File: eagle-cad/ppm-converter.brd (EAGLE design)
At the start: 48.3 x 49.5 mm, 22 parts, among them IC1 74HC14, IC2 74HC14, U1 ATMEGA328P, Y1 16Mhz

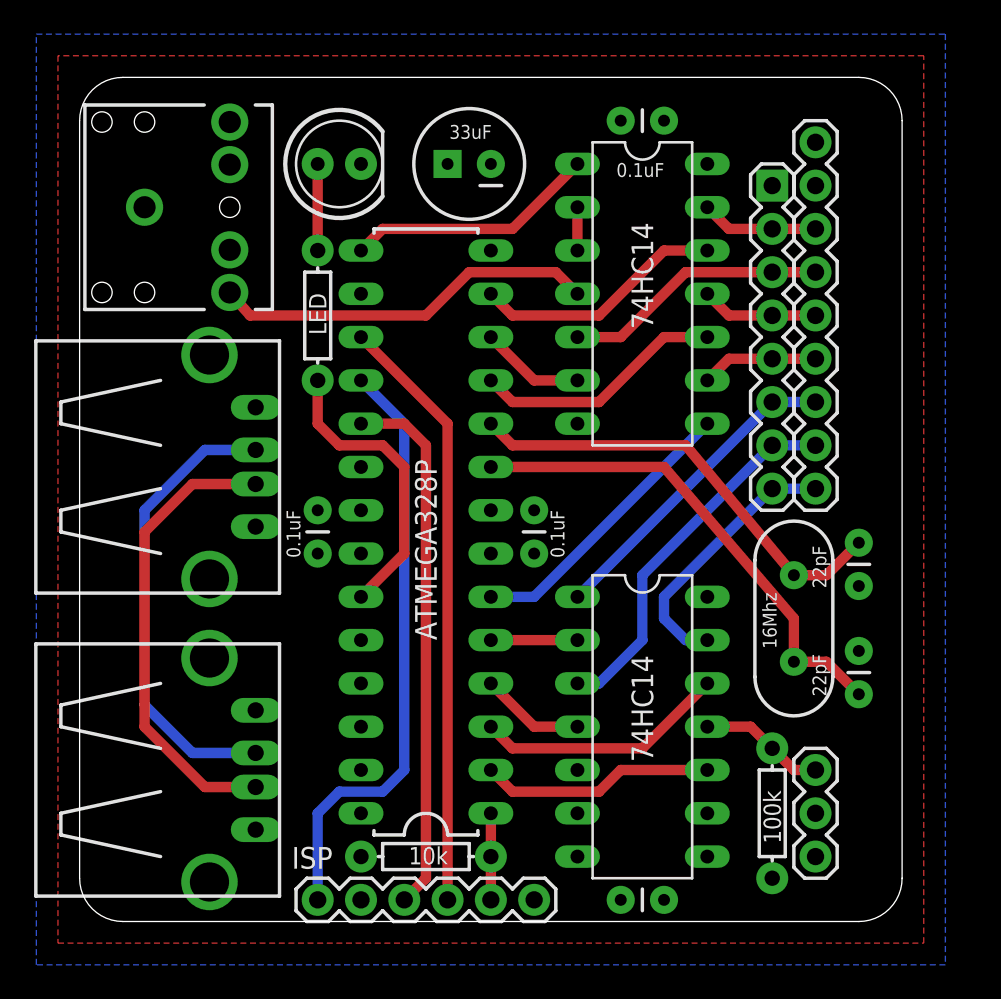
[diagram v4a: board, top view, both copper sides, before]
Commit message: A bit smaller board
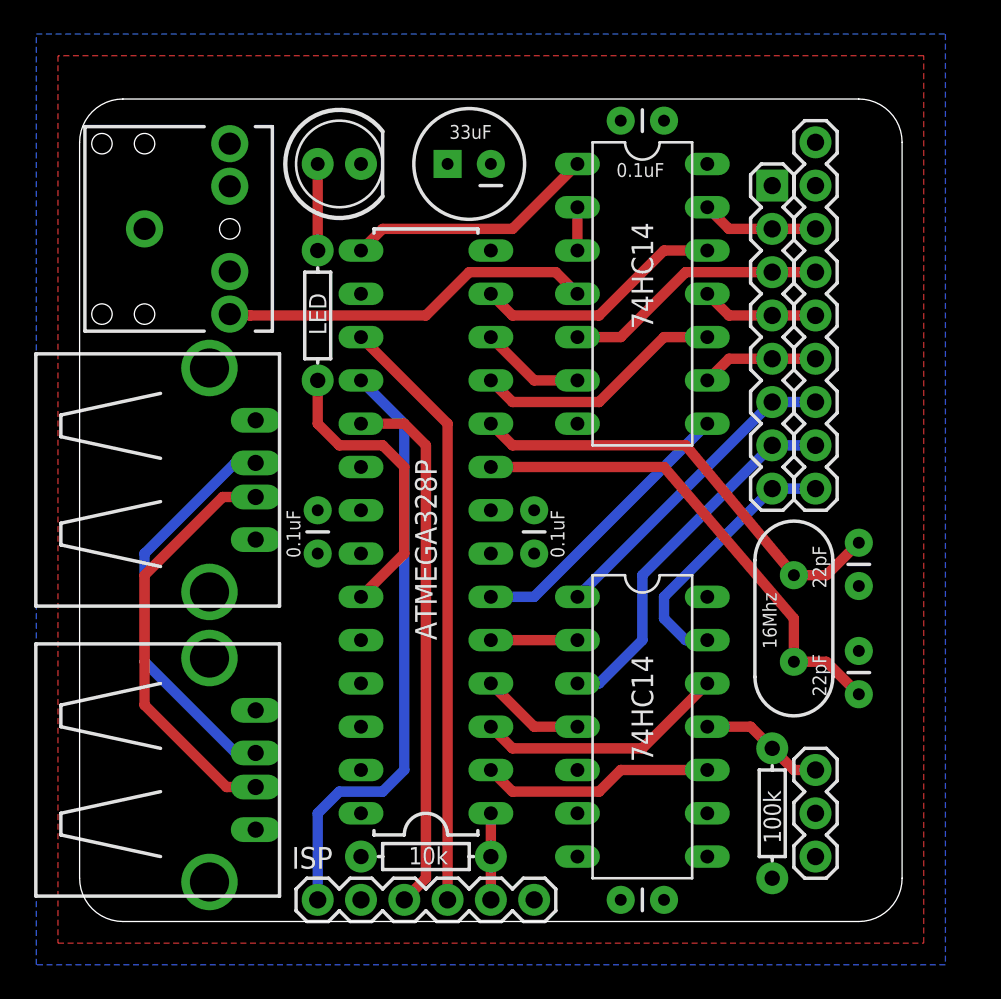
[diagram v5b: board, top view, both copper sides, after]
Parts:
- moved U2 1.27 mm to (3.81, 40.6)
- moved CN2 0.76 mm to (3.81, 25.9)
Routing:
- net N$2: track 27.1 -> 23.8 mm
- net N$3: track 27.1 -> 24.6 mm
- net N$8: track 22.6 -> 22.0 mm
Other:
- board size 48.3 x 49.5 mm -> 48.3 x 48.3 mm
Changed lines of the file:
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@@
 <text x="45.085" y="42.3164" size="2.54" layer="22" rot="MR90">+</text>
 <text x="45.085" y="44.8564" size="2.54" layer="22" rot="MR90">-</text>
-<text x="45.72" y="47.244" size="1.778" layer="26" rot="MR0">PWM</text>
+<text x="41.656" y="45.974" size="1.778" layer="26" rot="MR0">PWM</text>
 <text x="40.2082" y="2.3622" size="1.778" layer="26" rot="MR180">S.Bus</text>
 <text x="32.385" y="3.556" size="1.778" layer="26" rot="MR90">PWM/S.Bus to PPM -converter</text>
 <text x="19.558" y="9.398" size="1.778" layer="26" rot="MR90">Pertti Erkkilä 2013</text>
 <wire x1="2.54" y1="0" x2="45.72" y2="0" width="0" layer="20"/>
-<wire x1="48.26" y1="2.54" x2="48.26" y2="46.99" width="0" layer="20"/>
-<wire x1="45.72" y1="49.53" x2="2.54" y2="49.53" width="0" layer="20"/>
-<wire x1="0" y1="46.99" x2="0" y2="2.54" width="0" layer="20"/>
-<wire x1="0" y1="46.99" x2="2.54" y2="49.53" width="0" layer="20" curve="-90"/>
-<wire x1="45.72" y1="49.53" x2="48.26" y2="46.99" width="0" layer="20" curve="-90"/>
+<wire x1="48.26" y1="2.54" x2="48.26" y2="45.72" width="0" layer="20"/>
+<wire x1="45.72" y1="48.26" x2="2.54" y2="48.26" width="0" layer="20"/>
+<wire x1="0" y1="45.72" x2="0" y2="2.54" width="0" layer="20"/>
+<wire x1="0" y1="45.72" x2="2.54" y2="48.26" width="0" layer="20" curve="-90"/>
+<wire x1="45.72" y1="48.26" x2="48.26" y2="45.72" width="0" layer="20" curve="-90"/>
 <wire x1="48.26" y1="2.54" x2="45.72" y2="0" width="0" layer="20" curve="-90"/>
 <wire x1="2.54" y1="0" x2="0" y2="2.54" width="0" layer="20" curve="-90"/>
@@
 <attribute name="VALUE" x="32.385" y="15.621" size="1.27" layer="25" ratio="10" rot="R270"/>
 </element>
-<element name="U2" library="SparkFun-Connectors" package="AUDIO-JACK" value="" x="3.81" y="41.91" smashed="yes">
-<attribute name="VALUE" x="2.54" y="43.18" size="0.4064" layer="27"/>
+<element name="U2" library="SparkFun-Connectors" package="AUDIO-JACK" value="" x="3.81" y="40.64" smashed="yes">
+<attribute name="VALUE" x="2.54" y="41.91" size="0.4064" layer="27"/>
 </element>
 <element name="CN1" library="microbuilder" package="USB_HOST-PTH" value="" x="3.81" y="8.89" smashed="yes" rot="R270">
@@
 <attribute name="VALUE" x="46.355" y="2.54" size="1.27" layer="27" rot="R90"/>
 </element>
-<element name="CN2" library="microbuilder" package="USB_HOST-PTH" value="" x="3.81" y="26.67" smashed="yes" rot="R270">
-<attribute name="VALUE" x="-4.064" y="34.29" size="0.4064" layer="27" ratio="10" rot="R270"/>
+<element name="CN2" library="microbuilder" package="USB_HOST-PTH" value="" x="3.81" y="25.908" smashed="yes" rot="R270">
+<attribute name="VALUE" x="-4.064" y="33.528" size="0.4064" layer="27" ratio="10" rot="R270"/>
 </element>
 <element name="JP3" library="SparkFun-Connectors" package="1X09" value="M09" x="43.18" y="45.72" smashed="yes" rot="R270"/>
@@
 <contactref element="CN1" pad="D-"/>
 <contactref element="CN2" pad="D-"/>
-<wire x1="3.81" y1="12.7" x2="3.81" y2="24.13" width="0.6096" layer="16"/>
-<wire x1="3.81" y1="24.13" x2="7.35" y2="27.67" width="0.6096" layer="16"/>
-<wire x1="7.35" y1="27.67" x2="10.33" y2="27.67" width="0.6096" layer="16"/>
-<wire x1="3.81" y1="12.7" x2="6.62" y2="9.89" width="0.6096" layer="16"/>
-<wire x1="6.62" y1="9.89" x2="10.33" y2="9.89" width="0.6096" layer="16"/>
+<wire x1="3.81" y1="15.24" x2="3.81" y2="21.59" width="0.6096" layer="16"/>
+<wire x1="3.81" y1="15.24" x2="9.16" y2="9.89" width="0.6096" layer="16"/>
+<wire x1="9.16" y1="9.89" x2="10.33" y2="9.89" width="0.6096" layer="16"/>
+<wire x1="10.33" y1="26.908" x2="9.128" y2="26.908" width="0.6096" layer="16"/>
+<wire x1="9.128" y1="26.908" x2="3.81" y2="21.59" width="0.6096" layer="16"/>
 </signal>
 <signal name="N$3">
 <contactref element="CN1" pad="D+"/>
 <contactref element="CN2" pad="D+"/>
-<wire x1="3.81" y1="11.43" x2="3.81" y2="22.86" width="0.6096" layer="1"/>
-<wire x1="3.81" y1="22.86" x2="6.62" y2="25.67" width="0.6096" layer="1"/>
-<wire x1="6.62" y1="25.67" x2="10.33" y2="25.67" width="0.6096" layer="1"/>
-<wire x1="3.81" y1="11.43" x2="7.35" y2="7.89" width="0.6096" layer="1"/>
-<wire x1="7.35" y1="7.89" x2="10.33" y2="7.89" width="0.6096" layer="1"/>
+<wire x1="10.33" y1="24.908" x2="8.398" y2="24.908" width="0.6096" layer="1"/>
+<wire x1="8.398" y1="24.908" x2="3.81" y2="20.32" width="0.6096" layer="1"/>
+<wire x1="10.33" y1="7.89" x2="8.62" y2="7.89" width="0.6096" layer="1"/>
+<wire x1="8.62" y1="7.89" x2="3.81" y2="12.7" width="0.6096" layer="1"/>
+<wire x1="3.81" y1="12.7" x2="3.81" y2="20.32" width="0.6096" layer="1"/>
 </signal>
 <signal name="N$4">
@@
 <wire x1="22.86" y1="38.1" x2="20.32" y2="35.56" width="0.6096" layer="1"/>
 <wire x1="20.32" y1="35.56" x2="10" y2="35.56" width="0.6096" layer="1"/>
-<wire x1="10" y1="35.56" x2="8.81" y2="36.91" width="0.6096" layer="1"/>
+<wire x1="10" y1="35.56" x2="8.81" y2="35.64" width="0.6096" layer="1"/>
 </signal>
 <signal name="N$17">

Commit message: Minor fixes
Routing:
- net N$2: track 23.8 -> 24.6 mm
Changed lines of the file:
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@@
 <text x="45.085" y="44.8564" size="2.54" layer="22" rot="MR90">-</text>
 <text x="41.656" y="45.974" size="1.778" layer="26" rot="MR0">PWM</text>
-<text x="40.2082" y="2.3622" size="1.778" layer="26" rot="MR180">S.Bus</text>
+<text x="39.624" y="1.9558" size="1.778" layer="26" rot="MR180">S.Bus</text>
 <text x="32.385" y="3.556" size="1.778" layer="26" rot="MR90">PWM/S.Bus to PPM -converter</text>
 <text x="19.558" y="9.398" size="1.778" layer="26" rot="MR90">Pertti Erkkilä 2013</text>
@@
 <contactref element="C2" pad="2"/>
 <polygon width="0.6096" layer="16" isolate="0.4064">
-<vertex x="-2.54" y="52.07"/>
-<vertex x="50.8" y="52.07"/>
+<vertex x="-2.54" y="50.8"/>
+<vertex x="50.8" y="50.8"/>
 <vertex x="50.8" y="-2.54"/>
 <vertex x="-2.54" y="-2.54"/>
@@
 <contactref element="CN1" pad="D-"/>
 <contactref element="CN2" pad="D-"/>
-<wire x1="3.81" y1="15.24" x2="3.81" y2="21.59" width="0.6096" layer="16"/>
-<wire x1="3.81" y1="15.24" x2="9.16" y2="9.89" width="0.6096" layer="16"/>
-<wire x1="9.16" y1="9.89" x2="10.33" y2="9.89" width="0.6096" layer="16"/>
+<wire x1="3.81" y1="13.97" x2="3.81" y2="21.59" width="0.6096" layer="16"/>
+<wire x1="3.81" y1="13.97" x2="7.89" y2="9.89" width="0.6096" layer="16"/>
+<wire x1="7.89" y1="9.89" x2="10.33" y2="9.89" width="0.6096" layer="16"/>
 <wire x1="10.33" y1="26.908" x2="9.128" y2="26.908" width="0.6096" layer="16"/>
 <wire x1="9.128" y1="26.908" x2="3.81" y2="21.59" width="0.6096" layer="16"/>
@@
 <vertex x="-1.27" y="-1.27"/>
 <vertex x="49.53" y="-1.27"/>
-<vertex x="49.53" y="50.8"/>
-<vertex x="-1.27" y="50.8"/>
+<vertex x="49.53" y="49.53"/>
+<vertex x="-1.27" y="49.53"/>
 </polygon>
 <contactref element="IC1" pad="14"/>

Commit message: Finetuning for r02
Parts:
- moved R3 0.63 mm to (13.3, 35.6)
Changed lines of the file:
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@@
 <attribute name="VALUE" x="18.4404" y="42.6466" size="1.27" layer="27" ratio="10"/>
 </element>
-<element name="R3" library="SparkFun-Passives" package="AXIAL-0.3" value="LED" x="13.97" y="35.56" smashed="yes" rot="R270">
-<attribute name="VALUE" x="14.478" y="34.417" size="1.016" layer="21" font="vector" ratio="15" rot="R90"/>
+<element name="R3" library="SparkFun-Passives" package="AXIAL-0.3" value="LED" x="13.335" y="35.56" smashed="yes" rot="R270">
+<attribute name="VALUE" x="13.843" y="34.2392" size="1.016" layer="21" font="vector" ratio="15" rot="R90"/>
 </element>
 <element name="C5" library="SparkFun-Passives" package="CAP-PTH-SMALL" value="0.1uF" x="34.29" y="1.27" smashed="yes" rot="R180">
-<attribute name="VALUE" x="31.496" y="2.794" size="0.8128" layer="27"/>
+<attribute name="VALUE" x="31.496" y="2.794" size="0.8128" layer="25"/>
 </element>
 </elements>
@@
 <contactref element="R3" pad="P$1"/>
 <contactref element="LED" pad="A"/>
-<wire x1="13.97" y1="39.37" x2="13.97" y2="44.45" width="0.6096" layer="1"/>
+<wire x1="13.335" y1="39.37" x2="13.335" y2="43.815" width="0.6096" layer="1"/>
+<wire x1="13.335" y1="43.815" x2="13.97" y2="44.45" width="0.6096" layer="1"/>
 </signal>
 <signal name="N$31">
@@
 <wire x1="19.05" y1="26.67" x2="19.05" y2="21.59" width="0.6096" layer="1"/>
 <wire x1="19.05" y1="21.59" x2="16.51" y2="19.05" width="0.6096" layer="1"/>
-<wire x1="13.97" y1="31.75" x2="13.97" y2="29.21" width="0.6096" layer="1"/>
-<wire x1="13.97" y1="29.21" x2="15.24" y2="27.94" width="0.6096" layer="1"/>
+<wire x1="13.335" y1="31.75" x2="13.335" y2="29.845" width="0.6096" layer="1"/>
+<wire x1="13.335" y1="29.845" x2="15.24" y2="27.94" width="0.6096" layer="1"/>
 </signal>
 </signals>
